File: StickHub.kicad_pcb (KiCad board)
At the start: 2 copper layers, 16.5 x 40 mm, 94 parts, among them J1 HOST, J2 USB1, J3 USB2, J4 USB3, J5 USB4, J6 USB5, J7 USB6, J8 USB7, J9 EXTGND, U1 MaxLinear_XR22417-48, U2 Dialog_SLG5NT1487V, Y1 12MHz 50ppm 16-20pF

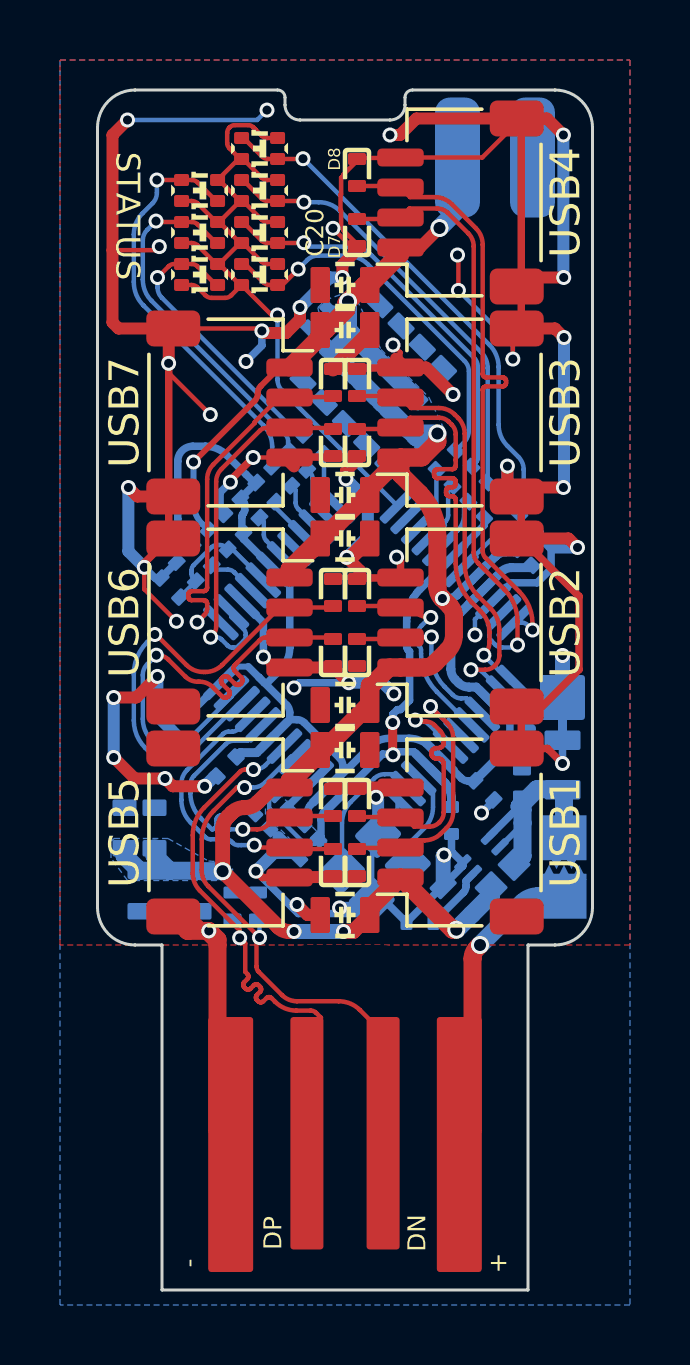
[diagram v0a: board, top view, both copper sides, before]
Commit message: Removing chunks of schematic and board.
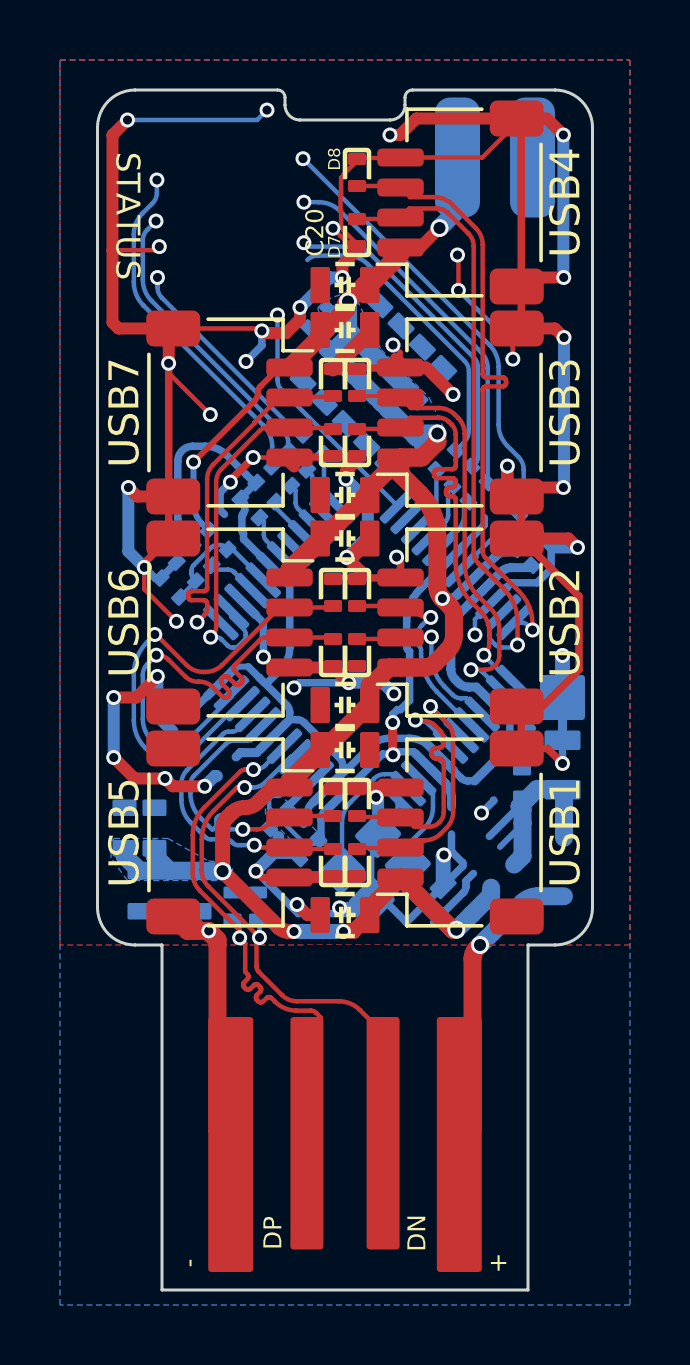
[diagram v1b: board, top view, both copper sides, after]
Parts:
- removed C10, C11, C12, C13, C5, C6, C7, C8, C9: 0.1uF, Capacitor_SMD:1005_C
- removed C28: 15nF, Capacitor_SMD:1005_C
- removed D15, D16, D17, D18, D19, D20, D21: USB, LED_SMD:Duo_LED_1.6x0.8_Kingbright_APHB1608LZGKSURKC
- removed JP1: EXTPWR, SH_Solder_Pads:JP-2_1.5x1.5
- removed U2: Dialog_SLG5NT1487V, Package_DFN_QFN:TDFN-8_1.5x2mm_Fused-Lead_JEDEC_MO-252_W2015D
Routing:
- net /LC: track 28.7 -> 8.19 mm
- net Net-(D15-1): track 12.7 -> 9.87 mm, vias 1 -> 0
- net Net-(D19-1): track 9.80 -> 7.34 mm
- net Net-(D16-1): track 13.3 -> 11.0 mm
- net Net-(D18-1): track 17.2 -> 14.9 mm
- net Net-(D17-1): track 14.7 -> 12.4 mm
- net Net-(D21-1): track 13.9 -> 11.6 mm
- net Net-(D20-1): track 12.1 -> 9.80 mm
- net Net-(U2-CAP): track 2.17 -> 0.00 mm
- net (no net): track 0.00 -> 2.17 mm
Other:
- board text removed: "StickHub"

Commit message: Revert "Removing chunks of schematic and board."
This reverts commit 6f6bff356a7eff26be86b812d608cab446a31a50.
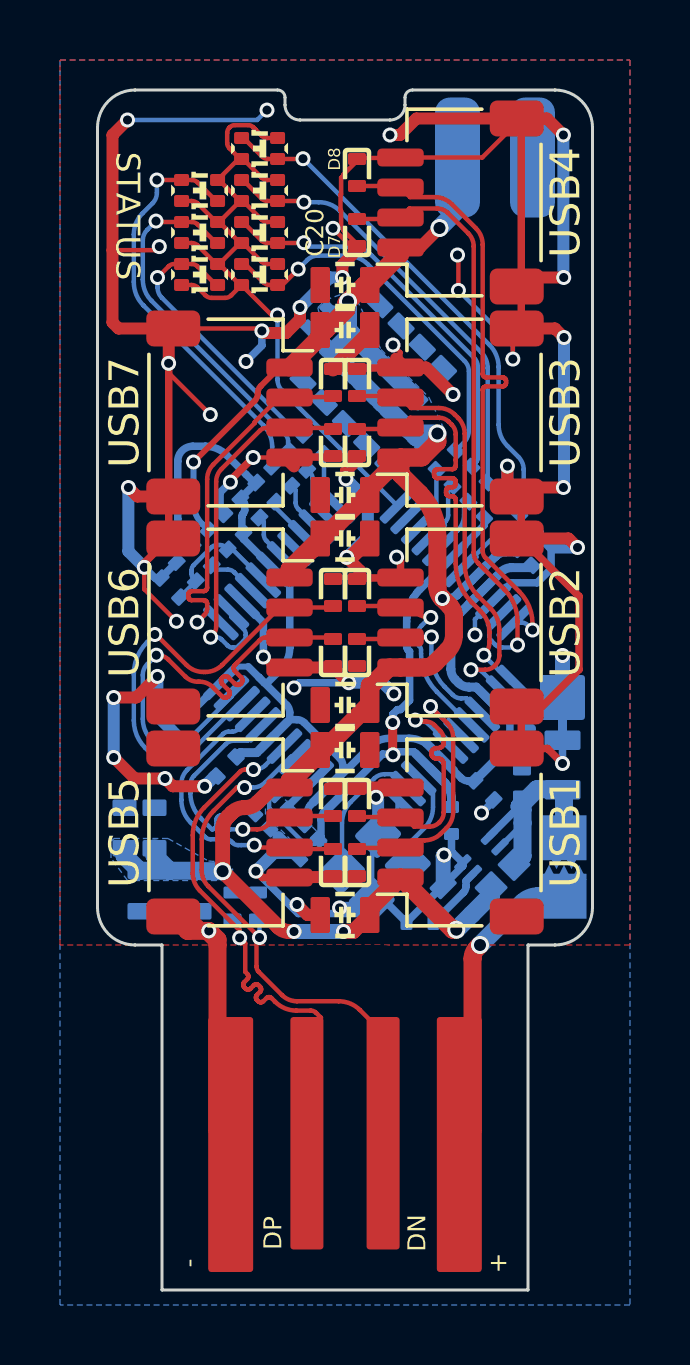
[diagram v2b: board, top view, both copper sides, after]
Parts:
- added C10: 0.1uF, Capacitor_SMD:1005_C, B.Cu at (154.6, 103.3)
- added C11: 0.1uF, Capacitor_SMD:1005_C, B.Cu at (155.0, 93.9)
- added C12: 0.1uF, Capacitor_SMD:1005_C, B.Cu at (153.6, 104.3)
- added C13: 0.1uF, Capacitor_SMD:1005_C, B.Cu at (147.3, 103.8)
- added C28: 15nF, Capacitor_SMD:1005_C, B.Cu at (152.5, 107.8)
- added C5: 0.1uF, Capacitor_SMD:1005_C, B.Cu at (148.3, 104.8)
- added C6: 0.1uF, Capacitor_SMD:1005_C, B.Cu at (146.1, 102.5)
- added C7: 0.1uF, Capacitor_SMD:1005_C, B.Cu at (144.6, 101.0)
- added C8: 0.1uF, Capacitor_SMD:1005_C, B.Cu at (155.8, 101.6)
- added C9: 0.1uF, Capacitor_SMD:1005_C, B.Cu at (146.3, 94.5)
- added D15: USB, LED_SMD:Duo_LED_1.6x0.8_Kingbright_APHB1608LZGKSURKC, F.Cu at (147.2, 86.2)
- added D16: USB, LED_SMD:Duo_LED_1.6x0.8_Kingbright_APHB1608LZGKSURKC, F.Cu at (147.2, 84.8)
- added D17: USB, LED_SMD:Duo_LED_1.6x0.8_Kingbright_APHB1608LZGKSURKC, F.Cu at (147.2, 83.3)
- added D18: USB, LED_SMD:Duo_LED_1.6x0.8_Kingbright_APHB1608LZGKSURKC, F.Cu at (147.2, 82.0)
- added D19: USB, LED_SMD:Duo_LED_1.6x0.8_Kingbright_APHB1608LZGKSURKC, F.Cu at (145.2, 86.2)
- added D20: USB, LED_SMD:Duo_LED_1.6x0.8_Kingbright_APHB1608LZGKSURKC, F.Cu at (145.2, 84.8)
- added D21: USB, LED_SMD:Duo_LED_1.6x0.8_Kingbright_APHB1608LZGKSURKC, F.Cu at (145.2, 83.3)
- added JP1: EXTPWR, SH_Solder_Pads:JP-2_1.5x1.5, B.Cu at (157.2, 105.9)
- added U2: Dialog_SLG5NT1487V, Package_DFN_QFN:TDFN-8_1.5x2mm_Fused-Lead_JEDEC_MO-252_W2015D, B.Cu at (154.9, 105.8)
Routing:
- net /LC: track 8.19 -> 28.7 mm
- net Net-(D15-1): track 9.87 -> 12.7 mm, vias 0 -> 1
- net Net-(D19-1): track 7.34 -> 9.80 mm
- net Net-(D16-1): track 11.0 -> 13.3 mm
- net Net-(D18-1): track 14.9 -> 17.2 mm
- net Net-(D17-1): track 12.4 -> 14.7 mm
- net Net-(D21-1): track 11.6 -> 13.9 mm
- net Net-(D20-1): track 9.80 -> 12.1 mm
- net Net-(U2-CAP): track 0.00 -> 2.17 mm
- net (no net): track 2.17 -> 0.00 mm
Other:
- board text added: "StickHub"
